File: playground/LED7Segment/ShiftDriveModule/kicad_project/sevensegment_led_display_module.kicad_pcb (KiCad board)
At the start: 2 copper layers, 47 x 33 mm, 11 parts, among them P1 CONN_01X05, U1 74HC595

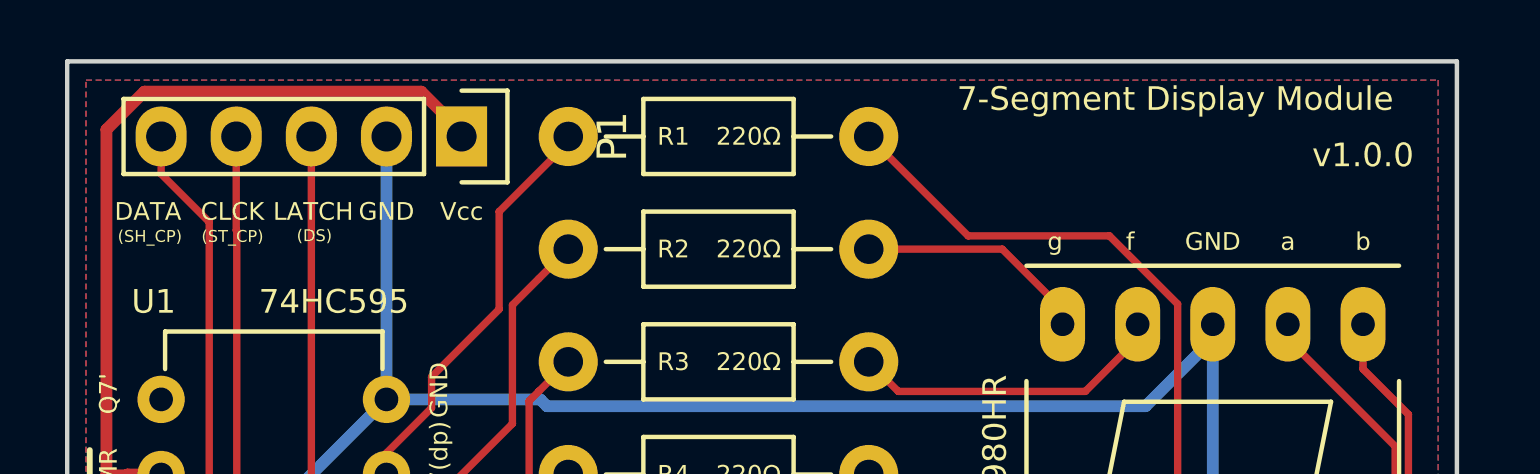
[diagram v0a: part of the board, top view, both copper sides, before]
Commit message: [LED7Segment/ShiftDriveModule] update now I have the PCBs from OSHPark
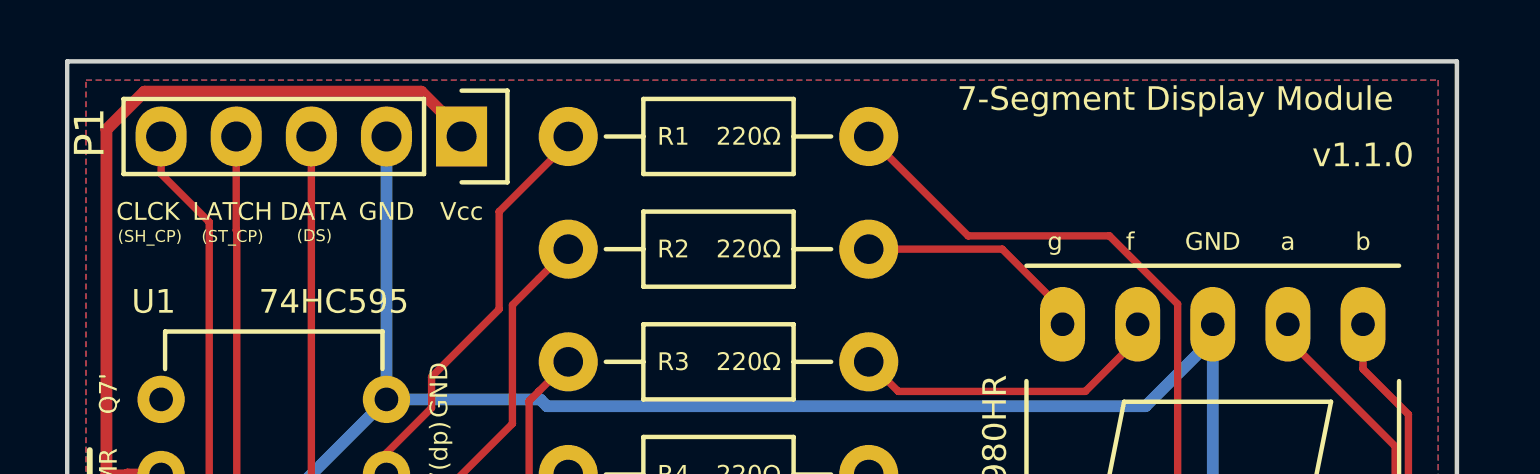
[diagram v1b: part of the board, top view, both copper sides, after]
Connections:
- P1 pad 3: /LATCH -> /DATA
- P1 pad 4: /CLK -> /LATCH
- P1 pad 5: /DATA -> /CLK
- U1 pad 11: /DATA -> /CLK
- U1 pad 12: /CLK -> /LATCH
- U1 pad 14: /LATCH -> /DATA
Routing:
- net /DATA: track 15.4 -> 23.7 mm
- net /LATCH: track 23.7 -> 17.6 mm
- net /CLK: track 17.6 -> 15.4 mm
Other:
- board text added: "v1.1.0"
- board text removed: "v1.0.0"
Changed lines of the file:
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@@
     (links 25)
     (no_connects 0)
-    (area 125.019999 88.945 172.160001 123.265001)
+    (area 124.632 88.945 172.160001 123.265001)
     (thickness 1.6)
     (drawings 44)
@@
     (title "Seven Segment Display Module")
     (date 2016-01-18)
-    (rev 1.0.0)
+    (rev 1.1.0)
     (company github.com/tardate/LittleArduinoProjects)
   )
@@
     (visible_elements FFFFFF7F)
     (pcbplotparams
-      (layerselection 0x090f0_80000001)
+      (layerselection 0x090fc_80000001)
       (usegerberextensions false)
       (excludeedgelayer true)
@@
     (descr "Through hole pin header")
     (tags "pin header")
-    (fp_text reference P1 (at 0 -5.1 270) (layer F.SilkS)
+    (fp_text reference P1 (at -0.127 12.573 270) (layer F.SilkS)
       (effects (font (size 1 1) (thickness 0.15)))
     )
@@
       (net 3 GND))
     (pad 3 thru_hole oval (at 0 5.08 270) (size 2.032 1.7272) (drill 1.016) (layers *.Cu *.Mask F.SilkS)
+      (net 13 /DATA))
+    (pad 4 thru_hole oval (at 0 7.62 270) (size 2.032 1.7272) (drill 1.016) (layers *.Cu *.Mask F.SilkS)
       (net 11 /LATCH))
-    (pad 4 thru_hole oval (at 0 7.62 270) (size 2.032 1.7272) (drill 1.016) (layers *.Cu *.Mask F.SilkS)
+    (pad 5 thru_hole oval (at 0 10.16 270) (size 2.032 1.7272) (drill 1.016) (layers *.Cu *.Mask F.SilkS)
       (net 12 /CLK))
-    (pad 5 thru_hole oval (at 0 10.16 270) (size 2.032 1.7272) (drill 1.016) (layers *.Cu *.Mask F.SilkS)
-      (net 13 /DATA))
     (model Pin_Headers.3dshapes/Pin_Header_Straight_1x05.wrl
       (at (xyz 0 -0.2 0))
@@
       (net 10 VCC))
     (pad 11 thru_hole oval (at 7.62 12.7 180) (size 1.6 1.6) (drill 0.8) (layers *.Cu *.Mask F.SilkS)
-      (net 13 /DATA))
+      (net 12 /CLK))
     (pad 12 thru_hole oval (at 7.62 10.16 180) (size 1.6 1.6) (drill 0.8) (layers *.Cu *.Mask F.SilkS)
-      (net 12 /CLK))
+      (net 11 /LATCH))
     (pad 13 thru_hole oval (at 7.62 7.62 180) (size 1.6 1.6) (drill 0.8) (layers *.Cu *.Mask F.SilkS)
       (net 3 GND))
     (pad 14 thru_hole oval (at 7.62 5.08 180) (size 1.6 1.6) (drill 0.8) (layers *.Cu *.Mask F.SilkS)
-      (net 11 /LATCH))
+      (net 13 /DATA))
     (pad 15 thru_hole oval (at 7.62 2.54 180) (size 1.6 1.6) (drill 0.8) (layers *.Cu *.Mask F.SilkS)
       (net 21 /ssA))
@@
     (effects (font (size 0.5 0.5) (thickness 0.125)))
   )
-  (gr_text v1.0.0 (at 168.91 93.345) (layer F.SilkS)
+  (gr_text v1.1.0 (at 168.91 93.345) (layer F.SilkS)
     (effects (font (size 0.8 0.8) (thickness 0.2)))
   )
@@
     (effects (font (size 0.6 0.6) (thickness 0.15)))
   )
-  (gr_text LATCH (at 133.4135 95.25) (layer F.SilkS)
-    (effects (font (size 0.6 0.6) (thickness 0.15)))
-  )
-  (gr_text CLCK (at 130.683 95.25) (layer F.SilkS)
-    (effects (font (size 0.6 0.6) (thickness 0.15)))
-  )
-  (gr_text DATA (at 127.8255 95.25) (layer F.SilkS)
+  (gr_text DATA (at 133.4135 95.25) (layer F.SilkS)
+    (effects (font (size 0.6 0.6) (thickness 0.15)))
+  )
+  (gr_text LATCH (at 130.683 95.25) (layer F.SilkS)
+    (effects (font (size 0.6 0.6) (thickness 0.15)))
+  )
+  (gr_text CLCK (at 127.8255 95.25) (layer F.SilkS)
     (effects (font (size 0.6 0.6) (thickness 0.15)))
   )
@@
   (segment (start 127.470001 118.580001) (end 128.27 119.38) (width 0.4) (layer F.Cu) (net 10))
   (segment (start 126.419989 117.529989) (end 127.470001 118.580001) (width 0.4) (layer F.Cu) (net 10))
-  (segment (start 133.35 92.71) (end 133.35 109.22) (width 0.25) (layer F.Cu) (net 11))
-  (segment (start 133.35 109.22) (end 128.27 114.3) (width 0.25) (layer F.Cu) (net 11))
-  (segment (start 130.81 95.879589) (end 130.828211 95.8978) (width 0.25) (layer F.Cu) (net 12))
-  (segment (start 130.81 92.71) (end 130.81 95.879589) (width 0.25) (layer F.Cu) (net 12))
-  (segment (start 130.828211 95.8978) (end 130.828211 106.661789) (width 0.25) (layer F.Cu) (net 12))
-  (segment (start 130.828211 106.661789) (end 129.069999 108.420001) (width 0.25) (layer F.Cu) (net 12))
-  (segment (start 129.069999 108.420001) (end 128.27 109.22) (width 0.25) (layer F.Cu) (net 12))
-  (segment (start 128.27 92.71) (end 128.27 93.976) (width 0.25) (layer F.Cu) (net 13))
-  (segment (start 128.27 93.976) (end 129.8956 95.6016) (width 0.25) (layer F.Cu) (net 13))
-  (segment (start 129.8956 95.6016) (end 129.8956 105.1052) (width 0.25) (layer F.Cu) (net 13))
-  (segment (start 128.27 106.7308) (end 128.27 106.68) (width 0.25) (layer F.Cu) (net 13))
-  (segment (start 129.8956 105.1052) (end 128.27 106.7308) (width 0.25) (layer F.Cu) (net 13))
+  (segment (start 130.81 95.879589) (end 130.828211 95.8978) (width 0.25) (layer F.Cu) (net 11))
+  (segment (start 130.81 92.71) (end 130.81 95.879589) (width 0.25) (layer F.Cu) (net 11))
+  (segment (start 130.828211 95.8978) (end 130.828211 106.661789) (width 0.25) (layer F.Cu) (net 11))
+  (segment (start 130.828211 106.661789) (end 129.069999 108.420001) (width 0.25) (layer F.Cu) (net 11))
+  (segment (start 129.069999 108.420001) (end 128.27 109.22) (width 0.25) (layer F.Cu) (net 11))
+  (segment (start 128.27 92.71) (end 128.27 93.976) (width 0.25) (layer F.Cu) (net 12))
+  (segment (start 128.27 93.976) (end 129.8956 95.6016) (width 0.25) (layer F.Cu) (net 12))
+  (segment (start 129.8956 95.6016) (end 129.8956 105.1052) (width 0.25) (layer F.Cu) (net 12))
+  (segment (start 128.27 106.7308) (end 128.27 106.68) (width 0.25) (layer F.Cu) (net 12))
+  (segment (start 129.8956 105.1052) (end 128.27 106.7308) (width 0.25) (layer F.Cu) (net 12))
+  (segment (start 133.35 92.71) (end 133.35 109.22) (width 0.25) (layer F.Cu) (net 13))
+  (segment (start 133.35 109.22) (end 128.27 114.3) (width 0.25) (layer F.Cu) (net 13))
   (segment (start 135.89 104.14) (end 135.89 103.413002) (width 0.25) (layer F.Cu) (net 14))
   (segment (start 139.7 95.25) (end 142.0368 92.9132) (width 0.25) (layer F.Cu) (net 14))
